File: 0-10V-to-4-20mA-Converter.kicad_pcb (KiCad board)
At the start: 2 copper layers, 48.7 x 24.8 mm, 15 parts, among them J1 Conn_01x02_Pin, J2 Conn_01x02_Pin, Q1 BCP56, U1 XTR116U, U2 MCP6002-I_SN

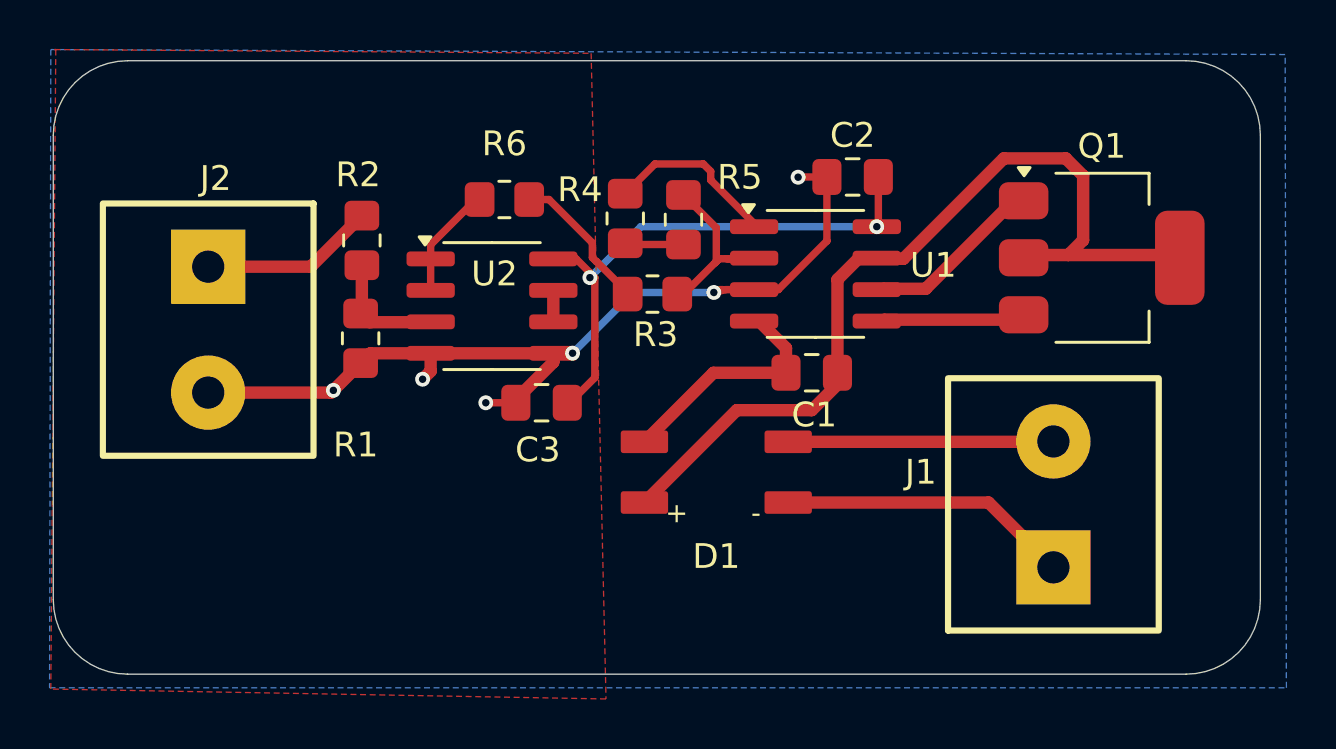
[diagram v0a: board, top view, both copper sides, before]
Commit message: Complete XTR116 PCB layout_DRC clean
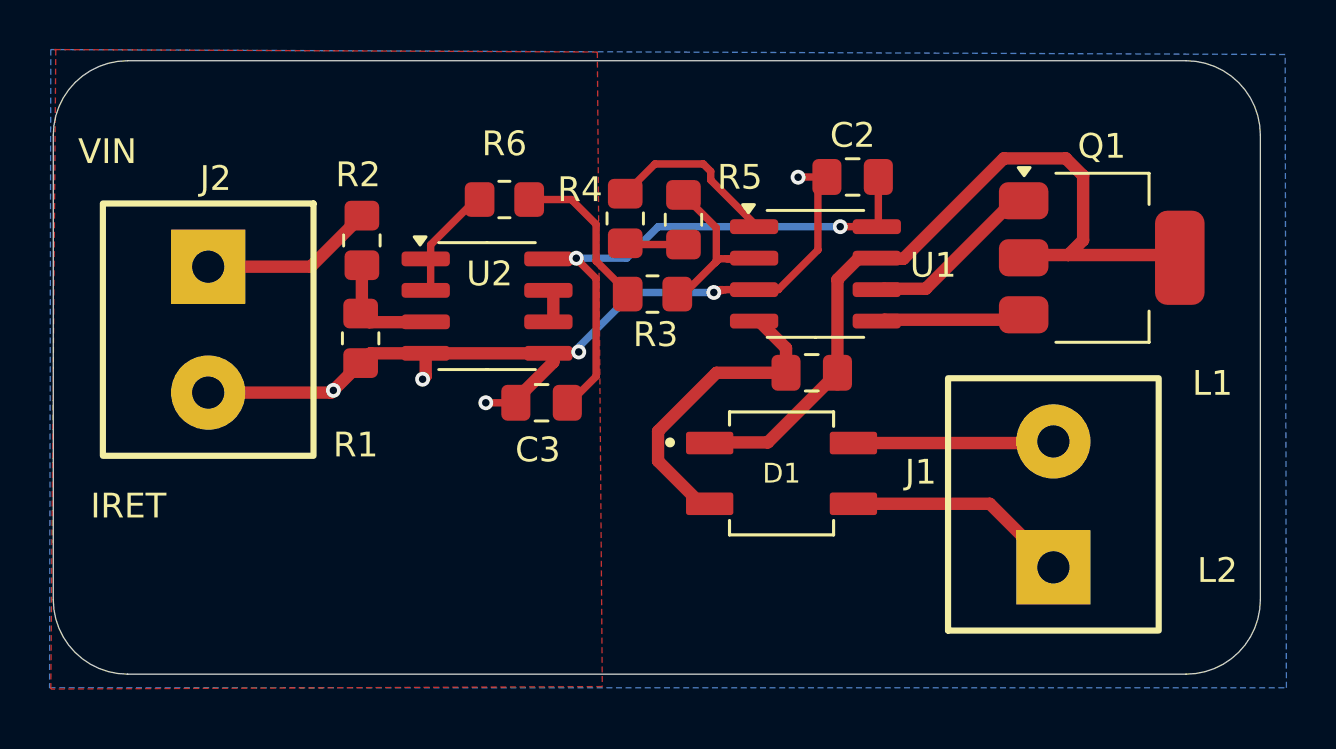
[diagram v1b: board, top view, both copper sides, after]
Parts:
- D1: footprint XTR116_Final_Footprints_MB10S_KF301:MB10S-13_Diodes_MBS -> MB10S:SOIC245P670X290-4N
- moved D1 2.63 mm to (119.6, 81.3), turned to 0 degrees
- moved U2 0.20 mm to (107.8, 74.6)
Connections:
- net Net-(J2-Pin_1) renamed /Vin
- net Net-(Q1-C) renamed /V+
- net Net-(U1-IIN) renamed /I_IN
- C1 pad 2: Net-(U1-IO) -> /IO
- D1 pad 2: Net-(U1-IO) -> Net-(J1-Pin_1)
- D1 pad 3: Net-(J1-Pin_1) -> /IO
- U1 pad 4: Net-(U1-IO) -> /IO
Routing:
- net /IO: track 0.00 -> 12.6 mm
- net Net-(U1-IO): track 9.37 -> 0.00 mm
- net /V+: track 36.0 -> 32.5 mm
- net Net-(J1-Pin_1): track 11.8 -> 9.13 mm
- net Net-(J1-Pin_2): track 10.7 -> 8.09 mm
- net /VREG_5V: track 22.0 -> 23.6 mm
- net /IRET_LOCAL: track 36.5 -> 37.5 mm
- net Net-(R3-Pad1): track 6.76 -> 7.28 mm
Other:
- board text added: "IRET"
- board text added: "L1"
- board text added: "L2"
- board text added: "VIN"

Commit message: completed Ver1
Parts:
- D1: footprint MB10S:SOIC245P670X290-4N -> MB10S:MB10S_DiodesInc
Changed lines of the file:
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@@
 		(allow_soldermask_bridges_in_footprints no)
 		(pcbplotparams
-			(layerselection 0x00010fc_ffffffff)
+			(layerselection 0x00010e0_ffffffff)
 			(plot_on_all_layers_selection 0x0000000_00000000)
 			(disableapertmacros no)
@@
 			(psa4output no)
 			(plotreference yes)
-			(plotvalue yes)
+			(plotvalue no)
 			(plotfptext yes)
 			(plotinvisibletext no)
 			(sketchpadsonfab no)
-			(subtractmaskfromsilk no)
+			(subtractmaskfromsilk yes)
 			(outputformat 1)
 			(mirror no)
-			(drillshape 1)
+			(drillshape 0)
 			(scaleselection 1)
-			(outputdirectory "")
+			(outputdirectory "geber/")
 		)
 	)
@@
 	(net 15 "/Vin")
 	(net 16 "/I_IN")
-	(footprint "MB10S:SOIC245P670X290-4N"
+	(footprint "MB10S:MB10S_DiodesInc"
 		(layer "F.Cu")
 		(at 119.6325 81.35)
@@
 			)
 		)
-		(property "Footprint" "MB10S:SOIC245P670X290-4N"
+		(property "Footprint" "MB10S:MB10S_DiodesInc"
 			(at 0 0 0)
 			(unlocked yes)
@@
 		(tags "resistor handsolder")
 		(property "Reference" "R3"
-			(at 0.125 1.635 360)
+			(at 0.125 1.635 0)
 			(layer "F.SilkS")
 			(effects
@@
 		)
 		(fp_text user "${REFERENCE}"
-			(at 0 0 360)
+			(at 0 0 0)
 			(layer "F.Fab")
 			(effects
@@
 		)
 		(fp_text user "${REFERENCE}"
-			(at 0 0 270)
+			(at 0 0 -90)
 			(layer "F.Fab")
 			(effects
@@
 		(tags "resistor handsolder")
 		(property "Reference" "R6"
-			(at 0 -2.25 360)
+			(at 0 -2.25 0)
 			(layer "F.SilkS")
 			(effects
@@
 		)
 		(property "Value" "10K"
-			(at -2.45 -1.7 360)
+			(at -2.45 -1.7 0)
 			(layer "F.Fab")
 			(effects
@@
 		)
 		(fp_text user "${REFERENCE}"
-			(at 0 0 360)
+			(at 0 0 0)
 			(layer "F.Fab")
 			(effects
@@
 		)
 		(property "Value" "Conn_01x02_Pin"
-			(at 2.54 5.15 270)
+			(at 2.54 5.15 -90)
 			(layer "F.Fab")
 			(effects
@@
 		(name "$teardrop_padvia$")
 		(hatch full 0.1)
-		(priority 30000)
+		(priority 30001)
 		(attr
 			(teardrop
@@
 		(polygon
 			(pts
-				(xy 105.525 76.979648) (xy 105.025 76.979648) (xy 104.872836 77.435195) (xy 105.15 77.551) (xy 105.45 77.55)
+				(xy 108.299997 78.65) (xy 108.299997 78.35) (xy 107.814802 78.222836) (xy 107.698997 78.5) (xy 107.814802 78.777164)
 			)
 		)
@@
 		(name "$teardrop_padvia$")
 		(hatch full 0.1)
-		(priority 30001)
+		(priority 30000)
 		(attr
 			(teardrop
@@
 		(polygon
 			(pts
-				(xy 108.299997 78.65) (xy 108.299997 78.35) (xy 107.814802 78.222836) (xy 107.698997 78.5) (xy 107.814802 78.777164)
+				(xy 105.525 76.979648) (xy 105.025 76.979648) (xy 104.872836 77.435195) (xy 105.15 77.551) (xy 105.45 77.55)
 			)
 		)
